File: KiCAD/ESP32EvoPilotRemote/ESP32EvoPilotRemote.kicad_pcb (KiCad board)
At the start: 2 copper layers, 69.8 x 50.8 mm, 13 parts, among them J1 433 MHz Transmitter, J2 D24V10F5, J3 Power, J3-1 Ant, J3-2 433MHz Receiver, J4 CAN-Transceiver, J5 Ant., J6 Ant., Q1 BC547, U1 esp32_38_pins

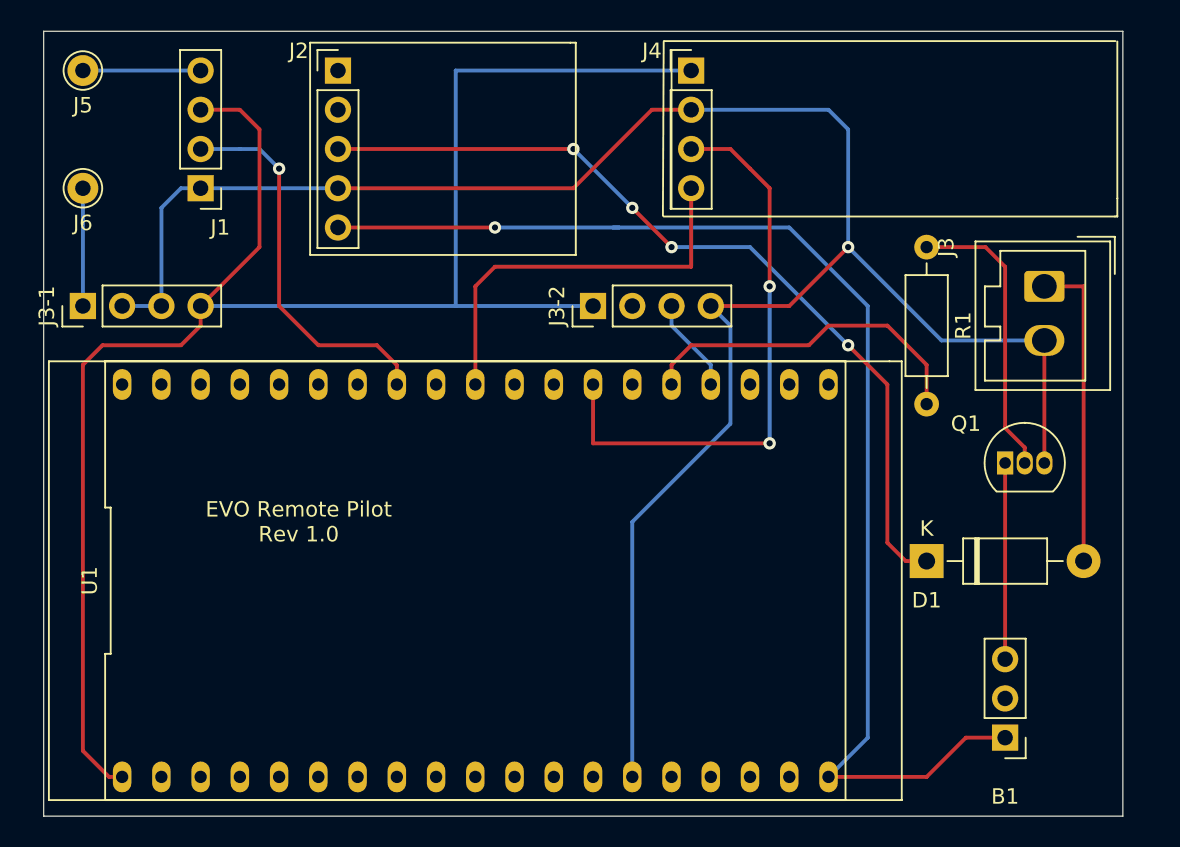
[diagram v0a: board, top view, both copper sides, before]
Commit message: Version 1.1
Bbigger terminal (5 mm) and other transistor footprint for easier soldering.
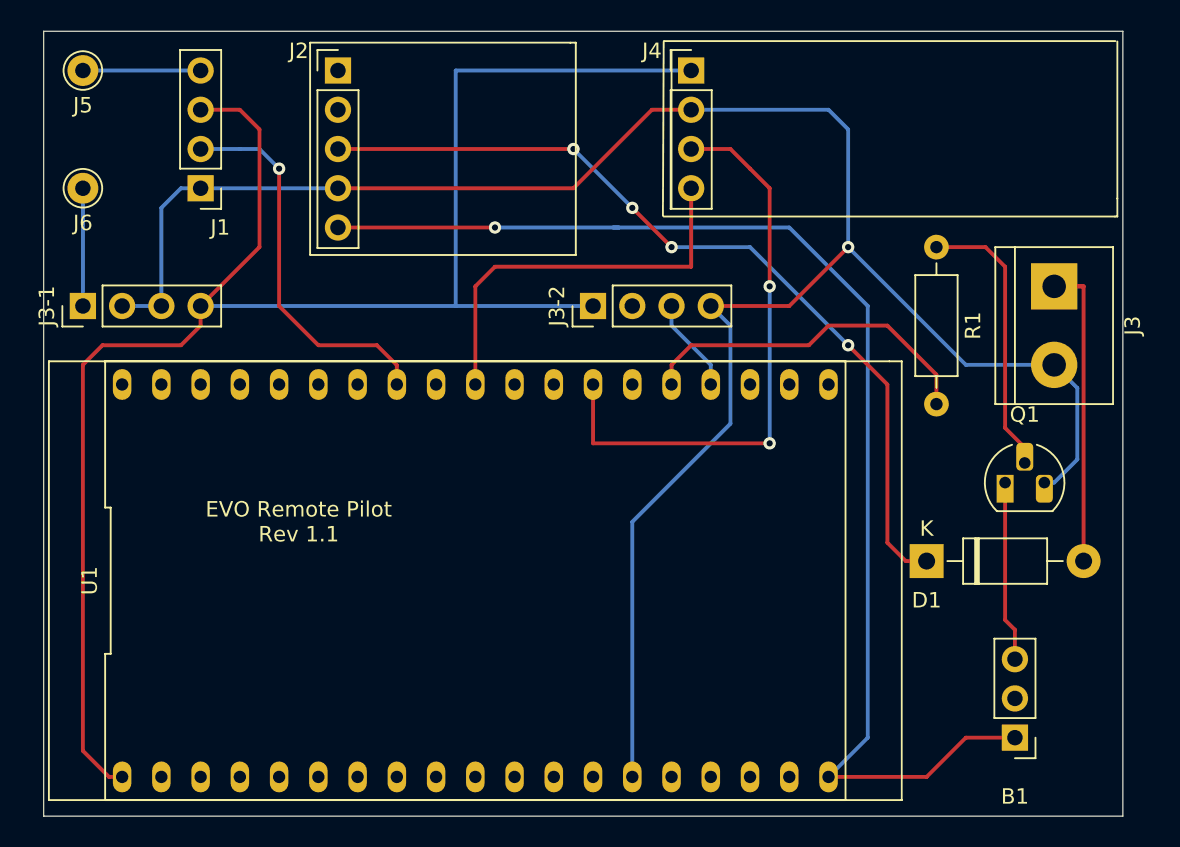
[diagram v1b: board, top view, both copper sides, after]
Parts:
- J3: footprint Connector_Wago:Wago_734-132_1x02_P3.50mm_Vertical -> TerminalBlock:TerminalBlock_bornier-2_P5.08mm
- Q1: footprint Package_TO_SOT_THT:TO-92_Inline -> Package_TO_SOT_THT:TO-92_HandSolder
- U1: footprint ESP32EvoPilotRemote2:esp32_dev4 -> ESP32_Devkit_38Pins:ESP32_Devkit_38Pins
- moved Q1 1.27 mm to (125.7, 124.5)
- moved B1 0.63 mm to (126.4, 141.0)
- moved J3 0.63 mm to (128.9, 111.8)
- moved R1 0.63 mm to (121.3, 109.2)
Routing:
- net GND: track 131.4 -> 135.1 mm
- net +12V: track 20.3 -> 22.2 mm
- net Net-(Q1-Pad2): track 18.8 -> 17.2 mm
- net Net-(B1-Pad3): track 12.7 -> 11.7 mm
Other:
- board text added: "EVO Remote Pilot Rev 1.1"
- board text removed: "EVO Remote Pilot Rev 1.0"

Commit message: Version 1.1
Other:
- board text added: "+12V"
- board text added: "GND"
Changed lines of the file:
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@@
   (general
     (thickness 1.6)
-    (drawings 17)
+    (drawings 19)
     (tracks 108)
     (zones 0)
@@
     (descr "simple 2-pin terminal block, pitch 5.08mm, revamped version of bornier2")
     (tags "terminal block bornier2")
-    (fp_text reference J3 (at 2.54 -5.08 90) (layer F.SilkS)
+    (fp_text reference J3 (at 2.54 -3.175 90) (layer F.SilkS)
       (effects (font (size 1 1) (thickness 0.15)))
     )
@@
     (fp_line (start -2.46 -3.75) (end -2.46 3.75) (layer F.Fab) (width 0.1))
     (fp_line (start -2.41 2.55) (end 7.49 2.55) (layer F.Fab) (width 0.1))
-    (fp_text user %R (at 2.54 0 90) (layer F.Fab)
+    (fp_text user %R (at 2.54 -3.175 90) (layer F.Fab)
       (effects (font (size 1 1) (thickness 0.15)))
     )
@@
     (descr "TO-92 leads molded, narrow, drill 0.75mm, handsoldering variant with enlarged pads (see NXP sot054_po.pdf)")
     (tags "to-92 sc-43 sc-43a sot54 PA33 transistor")
-    (fp_text reference Q1 (at 1.27 -4.4) (layer F.SilkS)
+    (fp_text reference Q1 (at -3.175 -0.635) (layer F.SilkS)
       (effects (font (size 1 1) (thickness 0.15)))
     )
@@
     (fp_line (start -0.5 1.75) (end 3 1.75) (layer F.Fab) (width 0.1))
     (fp_line (start -0.53 1.85) (end 3.07 1.85) (layer F.SilkS) (width 0.12))
-    (fp_text user %R (at 1.27 -4.4) (layer F.Fab)
+    (fp_text user %R (at -3.175 -0.635) (layer F.Fab)
       (effects (font (size 1 1) (thickness 0.15)))
     )
@@
     (descr "Resistor, Axial_DIN0207 series, Axial, Horizontal, pin pitch=10.16mm, 0.25W = 1/4W, length*diameter=6.3*2.5mm^2, http://cdn-reichelt.de/documents/datenblatt/B400/1_4W%23YAG.pdf")
     (tags "Resistor Axial_DIN0207 series Axial Horizontal pin pitch 10.16mm 0.25W = 1/4W length 6.3mm diameter 2.5mm")
-    (fp_text reference R1 (at 5.08 -2.37 90) (layer F.SilkS)
+    (fp_text reference R1 (at 5.08 0 90) (layer F.SilkS)
       (effects (font (size 1 1) (thickness 0.15)))
     )
@@
     )
   )
+  (gr_text GND (at 131.445 120.65) (layer F.SilkS)
+    (effects (font (size 1 1) (thickness 0.2)))
+  )
+  (gr_text +12V (at 130.81 107.95) (layer F.SilkS)
+    (effects (font (size 1 1) (thickness 0.2)))
+  )
   (gr_text "EVO Remote Pilot\nRev 1.1" (at 80.01 127) (layer F.SilkS)

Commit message: Version 1.2
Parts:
- turned U1 to 180 degrees
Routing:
- net Net-(R1-Pad2): track 22.7 -> 69.4 mm
- net Net-(J3-2-Pad3): track 6.13 -> 52.0 mm, vias 0 -> 1
- net Net-(J1-Pad2): track 25.0 -> 56.4 mm, vias 1 -> 2
- net Net-(J4-Pad4): track 25.9 -> 53.3 mm, vias 0 -> 1
- net Net-(J4-Pad3): track 37.9 -> 64.6 mm
- net +5V: track 80.8 -> 102.2 mm
- net GND: track 135.1 -> 116.0 mm
- net +3V3: track 111.4 -> 93.0 mm, vias 0 -> 1
- net Net-(U1-Pad4): track 0.00 -> 1.27 mm
- net Net-(U1-Pad12): track 0.00 -> 1.25 mm
- net Net-(U1-Pad20): track 0.00 -> 0.85 mm
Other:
- board text added: "EVO Remote Pilot Rev 1.2"
- board text removed: "EVO Remote Pilot Rev 1.1"
